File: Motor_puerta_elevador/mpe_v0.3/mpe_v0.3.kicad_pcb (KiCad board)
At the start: 2 copper layers, 201.1 x 147.9 mm, 34 parts, among them J1 IBT2, J10 ENCODER, J2 POWER, J3 MOTOR, J4 PROG, J5 IN1, J6 IN1, J7 IN1, J8 IN1, J9 IN1, P1 Power, P2 Analog, P3 Digital, P4 Digital, P5 CONN_01X01, P6 CONN_01X01, P7 CONN_01X01, P8 CONN_01X01, U1 ATmega3250PA-AU, U2 PC817, U3 PC817, U4 PC817, U5 PC817, U6 PC817

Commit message: ordenar pcb
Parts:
- added J11: IN+, Connector_Pin:Pin_D1.0mm_L10.0mm, F.Cu at (126.4, 24.8)
- added J12: IN+, Connector_Pin:Pin_D1.0mm_L10.0mm, F.Cu at (122.4, 33.3)
- added J13: IN-, Connector_Pin:Pin_D1.0mm_L10.0mm, F.Cu at (109.2, 24.8)
- added J14: IN-, Connector_Pin:Pin_D1.0mm_L10.0mm, F.Cu at (114.4, 33.3)
- added J15: OUT+, Connector_Pin:Pin_D1.0mm_L10.0mm, F.Cu at (126.4, 64.3)
- added J16: OUT+, Connector_Pin:Pin_D1.0mm_L10.0mm, F.Cu at (123.1, 55.2)
- added J17: OUT-, Connector_Pin:Pin_D1.0mm_L10.0mm, F.Cu at (109.2, 64.3)
- added J18: OUT-, Connector_Pin:Pin_D1.0mm_L10.0mm, F.Cu at (114.8, 55.2)
- moved J3 212.0 mm to (184.0, 51.4), turned to 270 degrees
- moved J2 207.4 mm to (184.0, 41.3), turned to 270 degrees
- moved J1 142.6 mm to (143.4, 57.8), turned to 180 degrees
- moved R4 87.0 mm to (103.6, 99.1), turned to 180 degrees
- moved U6 82.3 mm to (107.8, 114.3)
- moved U4 80.7 mm to (107.8, 99.1)
- moved R3 76.9 mm to (104.0, 91.4), turned to 180 degrees
- moved R5 75.7 mm to (103.4, 106.7), turned to 180 degrees
- moved R8 71.2 mm to (119.5, 99.1)
- moved R10 66.4 mm to (119.5, 114.3)
- moved R9 65.8 mm to (119.5, 106.7)
- moved R6 62.9 mm to (104.0, 114.3), turned to 180 degrees
- moved U2 62.3 mm to (107.8, 83.8)
- moved R1 60.8 mm to (104.0, 83.8), turned to 180 degrees
- moved J8 55.9 mm to (94.5, 110.5)
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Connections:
- J5 pad 1: +24V -> Earth
- J5 pad 3: Earth -> +24V
- J6 pad 1: +24V -> Earth
- J6 pad 3: Earth -> +24V
- J8 pad 1: +24V -> Earth
- J8 pad 3: Earth -> +24V
- J9 pad 1: +24V -> Earth
- J9 pad 3: Earth -> +24V
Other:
- board size 201.1 x 147.9 mm -> 99.7 x 110.5 mm

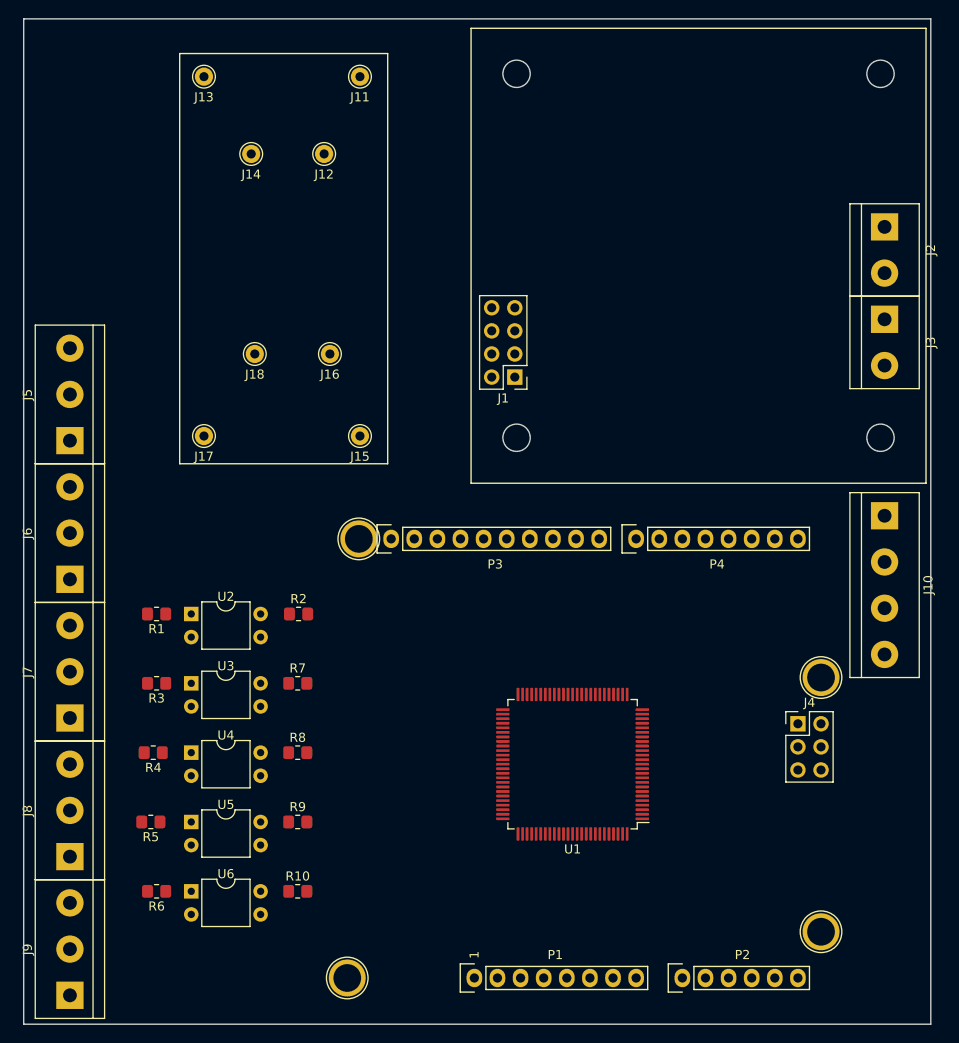
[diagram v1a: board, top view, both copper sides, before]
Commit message: agregar librerías y primeras pistas PCB
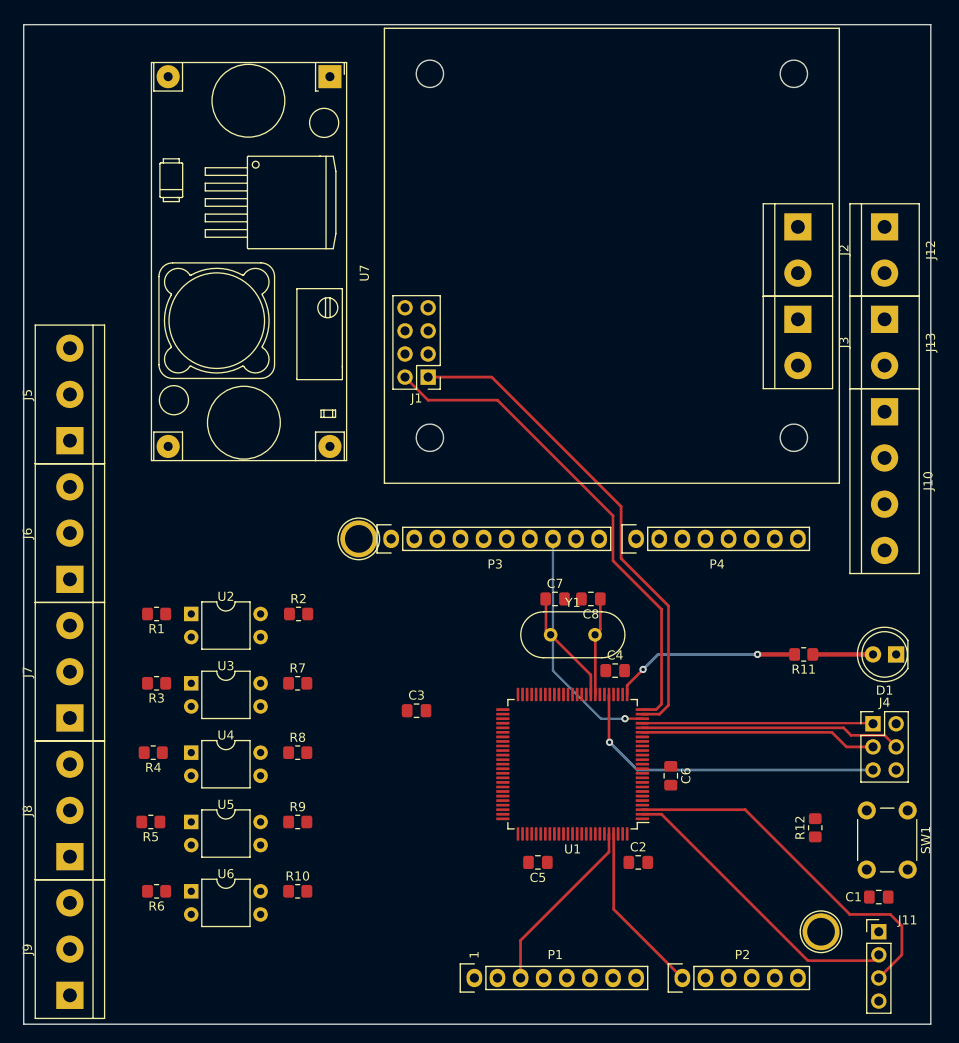
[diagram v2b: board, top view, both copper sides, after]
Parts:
- removed J14: IN-, Connector_Pin:Pin_D1.0mm_L10.0mm
- removed J15, J16: OUT+, Connector_Pin:Pin_D1.0mm_L10.0mm
- removed J17, J18: OUT-, Connector_Pin:Pin_D1.0mm_L10.0mm
- removed P5, P8: CONN_01X01, Socket_Arduino_Uno:Arduino_1pin
- added C1: 0.1u, Capacitor_SMD:C_0805_2012Metric_Pad1.18x1.45mm_HandSolder, F.Cu at (183.4, 114.9)
- added C2: 10u, Capacitor_SMD:C_0805_2012Metric_Pad1.18x1.45mm_HandSolder, F.Cu at (157.0, 111.1)
- added C3: 0.1u, Capacitor_SMD:C_0805_2012Metric_Pad1.18x1.45mm_HandSolder, F.Cu at (132.6, 94.5)
- added C4: 0.1u, Capacitor_SMD:C_0805_2012Metric_Pad1.18x1.45mm_HandSolder, F.Cu at (154.4, 90.0)
- added C5: 0.1u, Capacitor_SMD:C_0805_2012Metric_Pad1.18x1.45mm_HandSolder, F.Cu at (145.9, 111.1)
- added C6: 0.1u, Capacitor_SMD:C_0805_2012Metric_Pad1.18x1.45mm_HandSolder, F.Cu at (160.5, 101.6)
- added C7: 0.1u, Capacitor_SMD:C_0805_2012Metric_Pad1.18x1.45mm_HandSolder, F.Cu at (147.8, 82.2)
- added C8: 0.1u, Capacitor_SMD:C_0805_2012Metric_Pad1.18x1.45mm_HandSolder, F.Cu at (151.7, 82.2)
- added D1: LED, LED_THT:LED_D5.0mm, F.Cu at (185.3, 88.3)
- added R11: 330, Resistor_SMD:R_0805_2012Metric_Pad1.20x1.40mm_HandSolder, F.Cu at (175.1, 88.3)
- added R12: 10k, Resistor_SMD:R_0805_2012Metric_Pad1.20x1.40mm_HandSolder, F.Cu at (176.4, 107.3)
- added SW1: RESET, Button_Switch_THT:SW_PUSH_6mm, F.Cu at (186.6, 105.4)
- added U7: DCDC_StepDown, LM2596:YAAJ_DCDC_StepDown_LM2596, F.Cu at (123.1, 24.8)
- added Y1: 16M, Crystal:Crystal_HC49-4H_Vertical, F.Cu at (147.3, 86.1)
- J11: value IN+ -> Conn_01x04; footprint Connector_Pin:Pin_D1.0mm_L10.0mm -> Connector_PinHeader_2.54mm:PinHeader_1x04_P2.54mm_Vertical
- J12: value IN+ -> POWER; footprint Connector_Pin:Pin_D1.0mm_L10.0mm -> TerminalBlock:TerminalBlock_bornier-2_P5.08mm
- J13: value IN- -> MOTOR; footprint Connector_Pin:Pin_D1.0mm_L10.0mm -> TerminalBlock:TerminalBlock_bornier-2_P5.08mm
- moved J11 109.9 mm to (183.4, 118.7)
- moved J13 79.4 mm to (184.0, 51.4), turned to 270 degrees
- moved J12 62.1 mm to (184.0, 41.3), turned to 270 degrees
- moved J10 11.4 mm to (184.0, 61.6)
- moved J1 9.53 mm to (133.9, 57.8)
- moved J2 9.53 mm to (174.5, 41.3)
- moved J3 9.53 mm to (174.5, 51.4)
- moved J4 8.25 mm to (182.8, 95.9)
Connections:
- J11 pad 1: +24V -> +5V
- J12 pad 1: +24V -> Earth
- J13 pad 1: Earth -> Net-(J13-Pad1)
- J2 pad 1: Net-(J2-Pad1) -> Earth
- J2 pad 2: Net-(J2-Pad2) -> +24V
- J3 pad 1: Net-(J3-Pad1) -> Net-(J13-Pad1)
- J3 pad 2: Net-(J3-Pad2) -> Net-(J13-Pad2)
- U1 pad 10: Net-(U1-Pad10) -> +5V
- U1 pad 100: Net-(U1-Pad100) -> +5V
- U1 pad 11: Net-(U1-Pad11) -> GND
- U1 pad 2: Net-(U1-Pad2) -> Net-(J11-Pad2)
- U1 pad 3: Net-(U1-Pad3) -> Net-(J11-Pad3)
- U1 pad 30: Net-(U1-Pad30) -> /RST
- U1 pad 31: Net-(U1-Pad10) -> +5V
- U1 pad 32: Net-(U1-Pad11) -> GND
- U1 pad 80: Net-(U1-Pad10) -> +5V
- U1 pad 81: Net-(U1-Pad11) -> GND
- U1 pad 96: Net-(U1-Pad96) -> /Reset
- U1 pad 97: Net-(U1-Pad97) -> /A0
- U1 pad 99: Net-(U1-Pad99) -> GND
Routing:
- net /LPWM: track 0.00 -> 54.4 mm
- net /RPWM: track 0.00 -> 54.4 mm
- net Net-(J11-Pad3): track 0.00 -> 40.6 mm
- net /RST: track 0.00 -> 35.5 mm, vias 0 -> 1
- net Net-(J11-Pad2): track 0.00 -> 32.9 mm
- net /MOSI: track 0.00 -> 28.8 mm
- net /10(**SS): track 0.00 -> 27.4 mm, vias 0 -> 1
- net /SCK: track 0.00 -> 26.0 mm
- net /MISO: track 0.00 -> 25.4 mm
- net Net-(R11-Pad2): track 0.00 -> 20.8 mm, vias 0 -> 2
- net /Reset: track 0.00 -> 19.9 mm
- net /A0: track 0.00 -> 19.0 mm
- net Net-(C7-Pad1): track 0.00 -> 12.6 mm
- net Net-(C8-Pad1): track 0.00 -> 10.8 mm
- net Net-(D1-Pad2): track 0.00 -> 6.62 mm
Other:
- board size 99.7 x 110.5 mm -> 99.7 x 109.9 mm

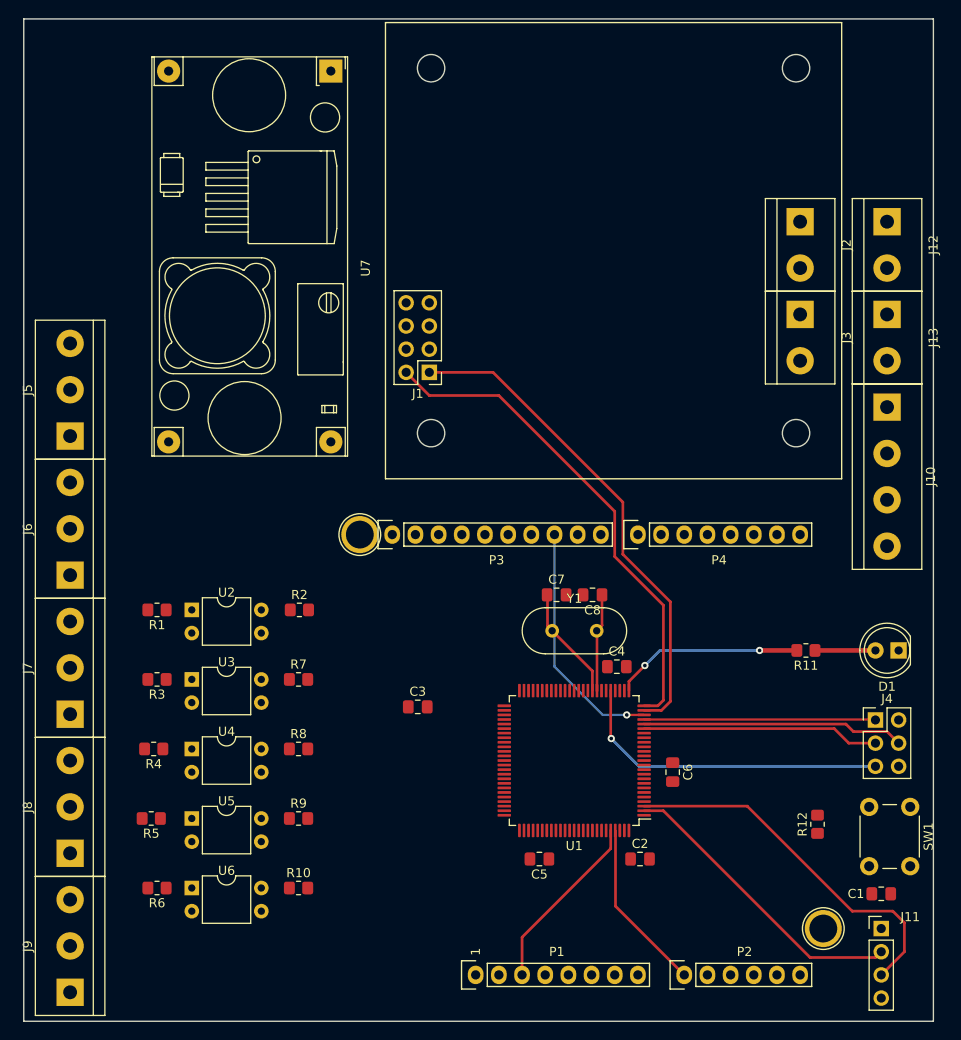
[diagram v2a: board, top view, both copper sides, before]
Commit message: PCB todo cableado
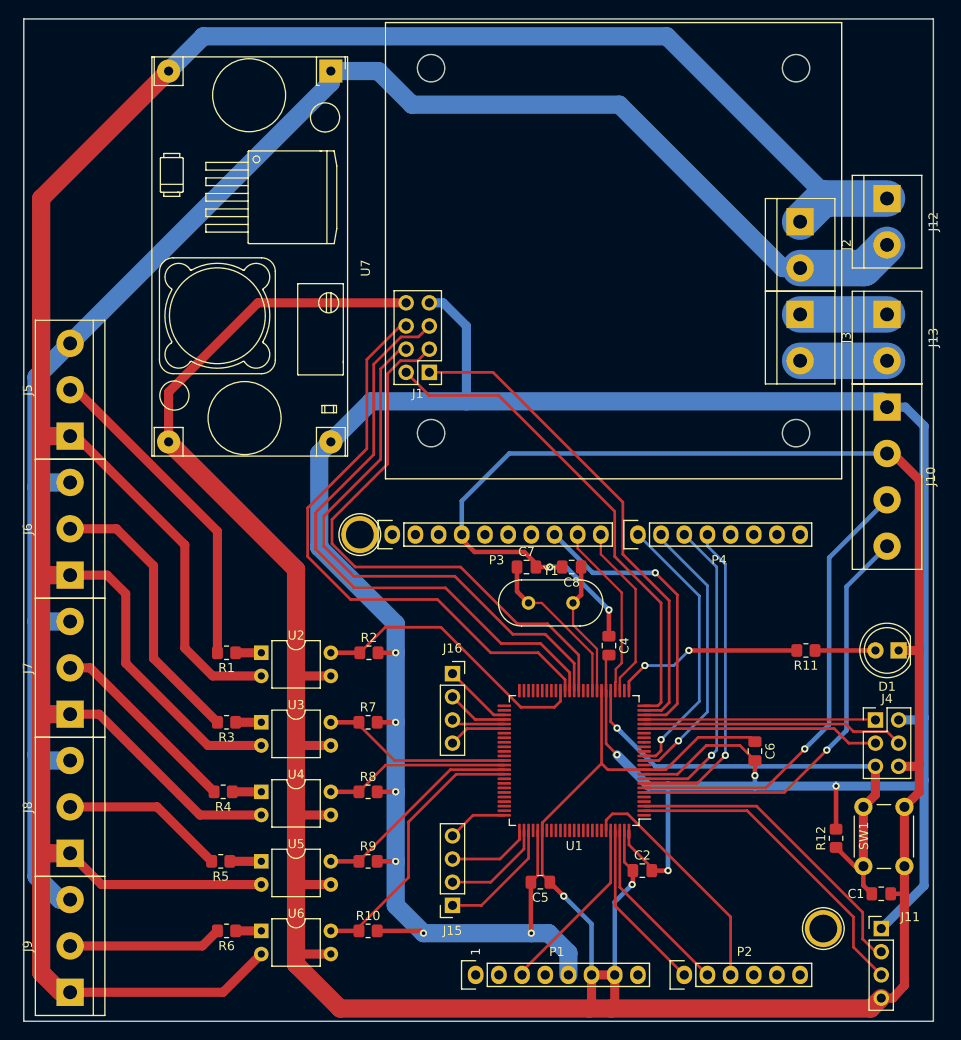
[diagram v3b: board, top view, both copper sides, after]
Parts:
- removed C3: 0.1u, Capacitor_SMD:C_0805_2012Metric_Pad1.18x1.45mm_HandSolder
- added J15: -, Connector_PinSocket_2.54mm:PinSocket_1x04_P2.54mm_Vertical, F.Cu at (136.4, 116.2)
- added J16: -, Connector_PinSocket_2.54mm:PinSocket_1x04_P2.54mm_Vertical, F.Cu at (136.4, 90.8)
- J11: value Conn_01x04 -> SERIAL
- J6: value IN1 -> IN2
- J7: value IN1 -> IN3
- J8: value IN1 -> IN4
- J9: value IN1 -> IN5
- R1, R3, R4, R5, R6: value 2.2k -> 10k
- moved C6 9.31 mm to (169.5, 99.3)
- moved R2 8.95 mm to (127.2, 88.5)
- moved U2 8.95 mm to (115.4, 88.5)
- moved R10 8.95 mm to (127.1, 119.0)
- moved R4 8.95 mm to (111.3, 103.8)
- moved R5 8.95 mm to (111.0, 111.4)
- moved R7 8.95 mm to (127.1, 96.1)
- moved R8 8.95 mm to (127.1, 103.8)
- moved R9 8.95 mm to (127.1, 111.4)
- moved U3 8.95 mm to (115.4, 96.1)
- moved U4 8.95 mm to (115.4, 103.8)
- moved U5 8.95 mm to (115.4, 111.4)
- moved U6 8.95 mm to (115.4, 119.0)
- moved R1 8.95 mm to (111.6, 88.5)
- moved R3 8.95 mm to (111.6, 96.1)
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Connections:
- net Net-(D1-Pad2) renamed /LED_
- net Net-(J13-Pad1) renamed /M1
- net Net-(J13-Pad2) renamed /M2
- net Net-(R11-Pad2) renamed /LED
- J10 pad 1: Net-(J10-Pad1) -> +5V
- J10 pad 2: Net-(J10-Pad2) -> GND
- J10 pad 3: Net-(J10-Pad3) -> /INTB(SDA)
- J10 pad 4: Net-(J10-Pad4) -> /INTA(SCL)
- J11 pad 2: Net-(J11-Pad2) -> /TX
- J11 pad 3: Net-(J11-Pad3) -> /RX
- J7 pad 1: +24V -> Earth
- J7 pad 3: Earth -> +24V
- P3 pad 1: /A5(SCL) -> /A5
- P3 pad 2: /A4(SDA) -> /A4
- R10 pad 1: Net-(R10-Pad1) -> /IN5
- R2 pad 1: Net-(R2-Pad1) -> /IN1
- R7 pad 1: Net-(R7-Pad1) -> /IN2
- R8 pad 1: Net-(R8-Pad1) -> /IN3
- R9 pad 1: Net-(R9-Pad1) -> /IN4
- U1 pad 13: Net-(U1-Pad13) -> /6(**)
- U1 pad 14: Net-(U1-Pad14) -> /7
- U1 pad 2: Net-(J11-Pad2) -> /RX
- U1 pad 28: Net-(U1-Pad28) -> /8
- U1 pad 29: Net-(U1-Pad29) -> /9(**)
- U1 pad 3: Net-(J11-Pad3) -> /TX
- U1 pad 37: Net-(U1-Pad37) -> /REN
- U1 pad 38: Net-(U1-Pad38) -> /LEN
- U1 pad 39: Net-(U1-Pad39) -> /RIS
- U1 pad 40: Net-(U1-Pad40) -> /LIS
- U1 pad 41: Net-(U1-Pad41) -> /IN1
- U1 pad 6: Net-(U1-Pad6) -> /INTA(SCL)
- U1 pad 63: Net-(U1-Pad63) -> /IN2
- U1 pad 64: Net-(U1-Pad64) -> /IN3
- U1 pad 65: Net-(U1-Pad65) -> /IN4
- U1 pad 66: Net-(U1-Pad66) -> /IN5
- U1 pad 7: Net-(U1-Pad7) -> /INTB(SDA)
- U1 pad 8: Net-(U1-Pad8) -> /4
- U1 pad 9: Net-(U1-Pad9) -> /5(**)
- U1 pad 95: Net-(U1-Pad95) -> /A2
- U1 pad 98: Net-(U1-Pad98) -> /A1
- U2 pad 4: Net-(R2-Pad1) -> /IN1
- U3 pad 4: Net-(R7-Pad1) -> /IN2
- U4 pad 4: Net-(R8-Pad1) -> /IN3
- U5 pad 4: Net-(R9-Pad1) -> /IN4
- U6 pad 4: Net-(R10-Pad1) -> /IN5
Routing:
- net GND: track 0.00 -> 413.8 mm, vias 0 -> 4
- net Earth: track 0.00 -> 362.0 mm
- net +5V: track 0.00 -> 330.7 mm, vias 0 -> 10
- net +24V: track 0.00 -> 188.8 mm
- net /RIS: track 0.00 -> 66.2 mm
- net /LIS: track 0.00 -> 65.1 mm
- net /REN: track 0.00 -> 62.9 mm
- net /LEN: track 0.00 -> 61.4 mm
- net /INTB(SDA): track 0.00 -> 50.4 mm, vias 0 -> 1
- net /INTA(SCL): track 0.00 -> 47.0 mm, vias 0 -> 1
- net Net-(J11-Pad3): track 40.6 -> 0.00 mm
- net Net-(J5-Pad2): track 0.00 -> 35.9 mm
- net /RX: track 0.00 -> 35.4 mm
- net /4: track 0.00 -> 35.2 mm, vias 0 -> 1
- net /5(**): track 0.00 -> 34.4 mm, vias 0 -> 1
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
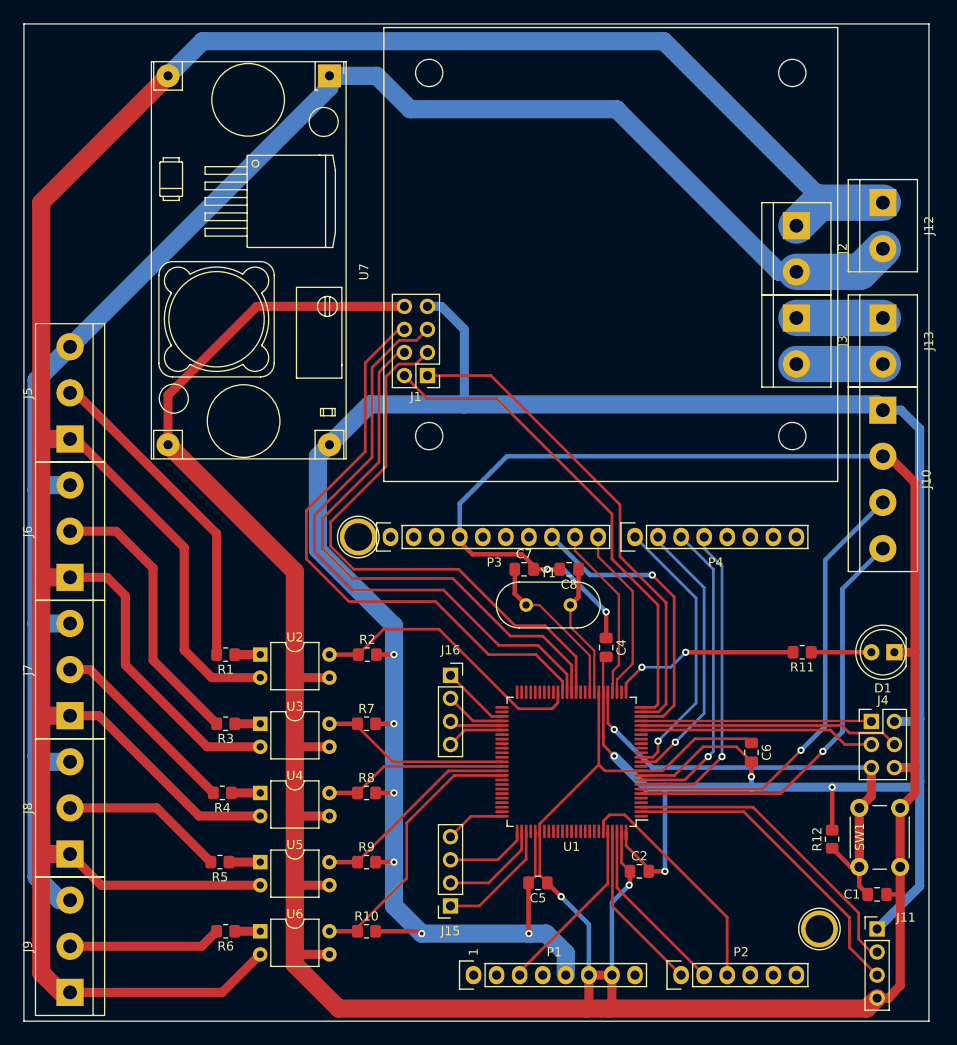
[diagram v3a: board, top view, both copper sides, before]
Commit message: reconectar entradas analógicas
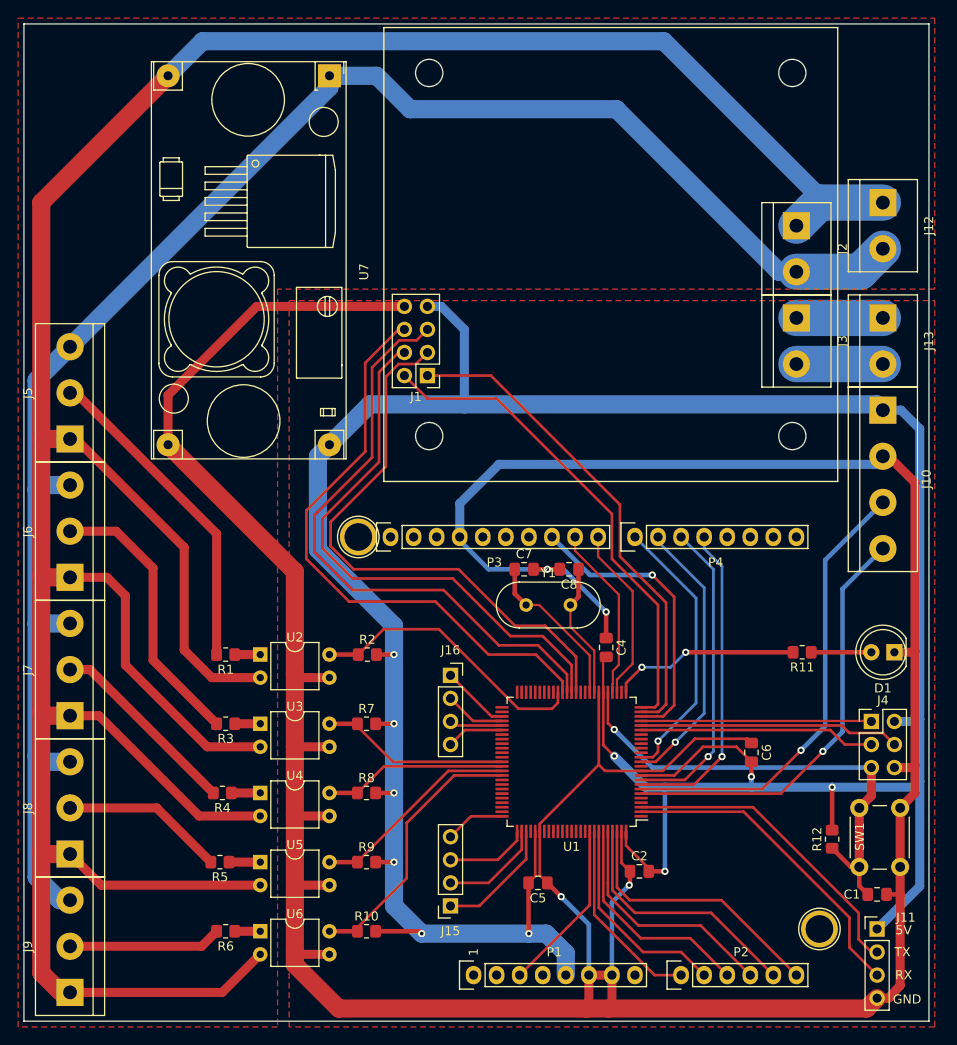
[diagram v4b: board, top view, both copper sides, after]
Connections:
- U1 pad 92: Net-(U1-Pad92) -> /Reset
- U1 pad 93: Net-(U1-Pad93) -> /A0
- U1 pad 94: Net-(U1-Pad94) -> /A1
- U1 pad 96: /Reset -> /A3
- U1 pad 97: /A0 -> /A4(SDA)
- U1 pad 98: /A1 -> /A5(SCL)
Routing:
- net /A5(SCL): track 0.00 -> 29.9 mm
- net /A4(SDA): track 0.00 -> 28.1 mm
- net /A3: track 0.00 -> 26.3 mm
- net /A1: track 19.8 -> 23.1 mm
- net /A0: track 19.0 -> 21.5 mm
- net /A2: track 26.1 -> 24.0 mm
- net GND: track 413.8 -> 415.0 mm
- added copper zone on F.Cu, net Earth
- added copper zone on F.Cu, net GND
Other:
- board text added: "5V"
- board text added: "GND"
- board text added: "RX"
- board text added: "TX"
